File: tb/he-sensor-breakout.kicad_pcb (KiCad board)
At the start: 2 copper layers, 19.1 x 17.8 mm, 28 parts, among them J1 Conn_01x01_Pin, J10 Conn_01x01_Pin, J11 Conn_01x01_Pin, J12 Conn_01x01_Pin, J13 Conn_01x01_Pin, J14 Conn_01x01_Pin, J2 Conn_01x01_Pin, J3 Conn_01x01_Pin, J4 Conn_01x01_Pin, J5 Conn_01x01_Pin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

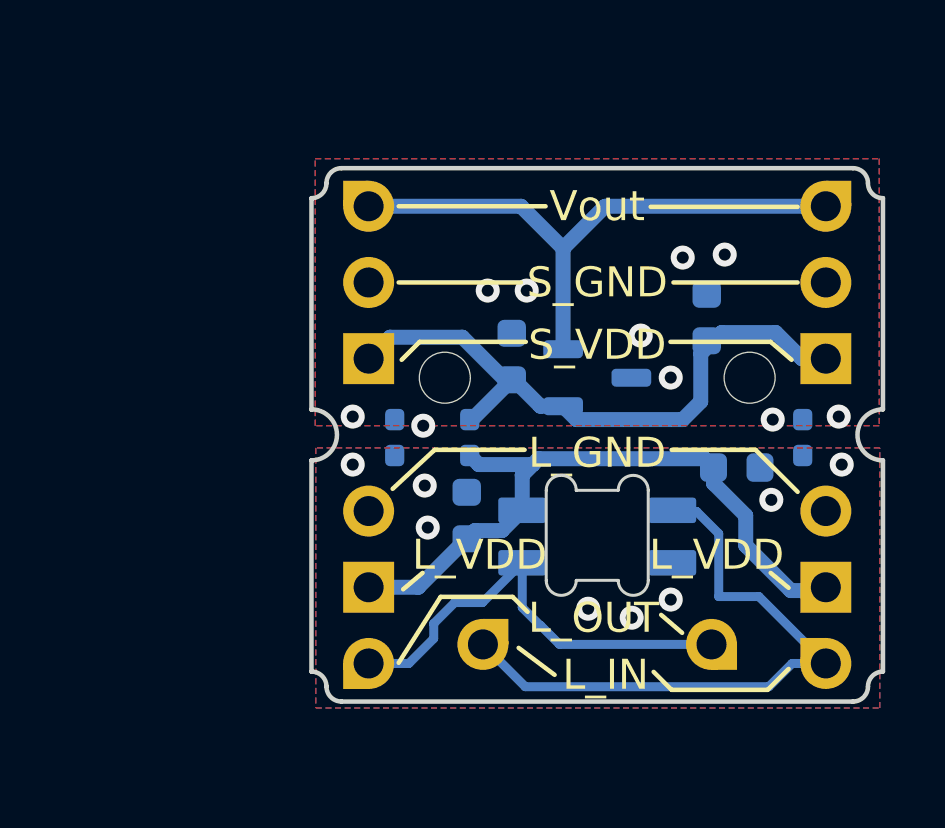
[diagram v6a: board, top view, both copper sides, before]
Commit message: fix edge cuts
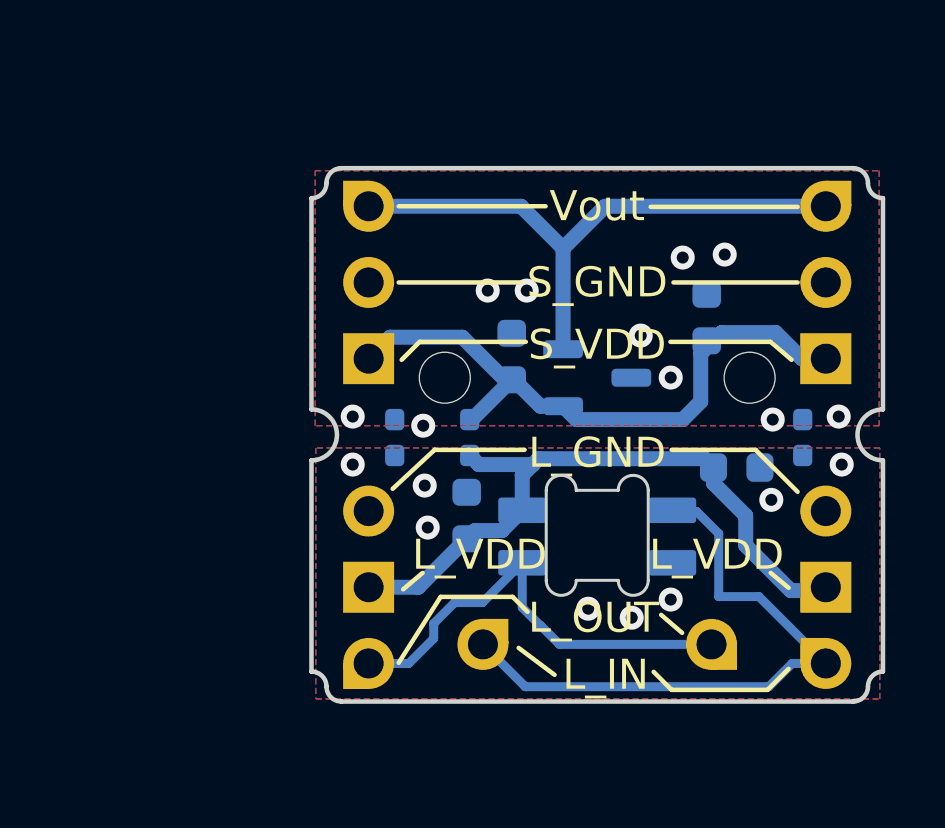
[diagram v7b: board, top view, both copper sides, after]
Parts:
- added REF**: Tab, kikit:Tab, F.Cu at (99.1, 97.2)
- added REF**: Tab, kikit:Tab, F.Cu at (99.1, 106.0)
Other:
- outline, holes or cut-outs redrawn
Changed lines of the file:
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@@
         (effects (font (size 1.2 1.2) (thickness 0.2)))
     )
-    (fp_text user "KIKIT: width: 6.5mm" (at -6.7 2.0275 180) (layer "Dwgs.User")
+    (fp_text user "KIKIT: width: 6mm" (at -6.7 2.0275 180) (layer "Dwgs.User")
         (effects (font (size 1 1) (thickness 0.15)))
     )
@@
   )
   (footprint "kikit:Tab" (layer "F.Cu")
-    (at 120.22 97.2225 180)
+    (at 99.06 97.23)
     (descr "A symbol representing annotation for tab placement")
     (attr exclude_from_pos_files exclude_from_bom)
@@
         (effects (font (size 1.2 1.2) (thickness 0.2)))
     )
-    (fp_text user "KIKIT: width: 6.5mm" (at -6.7 2.0275 180) (layer "Dwgs.User")
+    (fp_text user "KIKIT: width: 6mm" (at -6.7 2.0275) (layer "Dwgs.User")
+        (effects (font (size 1 1) (thickness 0.15)))
+    )
+    (fp_line (start 0.25 0) (end -2.75 0)
+      (stroke (width 0.3) (type solid)) (layer "Dwgs.User"))
+    (fp_line (start 0.25 0) (end -0.75 -1)
+      (stroke (width 0.3) (type solid)) (layer "Dwgs.User"))
+    (fp_line (start 0.25 0) (end -0.75 1)
+      (stroke (width 0.3) (type solid)) (layer "Dwgs.User"))
+    (fp_line (start 0.25 1) (end 0.25 -1)
+      (stroke (width 0.3) (type solid)) (layer "Dwgs.User"))
+  )
+  (footprint "kikit:Tab" (layer "F.Cu")
+    (at 99.06 105.97)
+    (descr "A symbol representing annotation for tab placement")
+    (attr exclude_from_pos_files exclude_from_bom)
+    (fp_text reference "REF**" (at 0 -2) (layer "F.SilkS") hide
+        (effects (font (size 1 1) (thickness 0.15)))
+    )
+    (fp_text value "Tab" (at -3 -1.0725) (layer "Dwgs.User")
+        (effects (font (size 1.2 1.2) (thickness 0.2)))
+    )
+    (fp_text user "KIKIT: width: 6mm" (at -6.7 2.0275) (layer "Dwgs.User")
+        (effects (font (size 1 1) (thickness 0.15)))
+    )
+    (fp_line (start 0.25 0) (end -2.75 0)
+      (stroke (width 0.3) (type solid)) (layer "Dwgs.User"))
+    (fp_line (start 0.25 0) (end -0.75 -1)
+      (stroke (width 0.3) (type solid)) (layer "Dwgs.User"))
+    (fp_line (start 0.25 0) (end -0.75 1)
+      (stroke (width 0.3) (type solid)) (layer "Dwgs.User"))
+    (fp_line (start 0.25 1) (end 0.25 -1)
+      (stroke (width 0.3) (type solid)) (layer "Dwgs.User"))
+  )
+  (footprint "kikit:Tab" (layer "F.Cu")
+    (at 120.22 97.23 180)
+    (descr "A symbol representing annotation for tab placement")
+    (attr exclude_from_pos_files exclude_from_bom)
+    (fp_text reference "REF**" (at 0 -2) (layer "F.SilkS") hide
+        (effects (font (size 1 1) (thickness 0.15)))
+    )
+    (fp_text value "Tab" (at -3 -1.0725) (layer "Dwgs.User")
+        (effects (font (size 1.2 1.2) (thickness 0.2)))
+    )
+    (fp_text user "KIKIT: width: 6mm" (at -6.7 2.0275 180) (layer "Dwgs.User")
         (effects (font (size 1 1) (thickness 0.15)))
     )
@@
   (gr_arc (start 118.745 102.45) (mid 117.895 101.6) (end 118.745 100.75)
     (stroke (width 0.15) (type default)) (layer "Edge.Cuts"))
-  (gr_line (start 99.695 93.71) (end 99.695 100.765)
+  (gr_line (start 99.695 93.71) (end 99.695 100.75)
     (stroke (width 0.15) (type default)) (layer "Edge.Cuts"))
   (gr_line (start 117.745 110.49) (end 100.695 110.49)
@@
       (pts
         (xy 99.84 102.034567)
-        (xy 99.84 110.704567)
-        (xy 118.64 110.704567)
+        (xy 99.84 110.404567)
+        (xy 118.64 110.404567)
         (xy 118.64 102.034567)
       )
@@
     (polygon
       (pts
-        (xy 99.82 92.394567)
-        (xy 118.62 92.394567)
+        (xy 99.82 92.794567)
+        (xy 118.62 92.794567)
         (xy 118.62 101.294567)
         (xy 99.82 101.294567)

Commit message: remove duplicate tabs
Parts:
- removed the REF** at (99.1, 97.2)
- removed the REF** at (99.1, 106.0)
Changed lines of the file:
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@@
-  )
-  (footprint "kikit:Tab" (layer "F.Cu")
-    (at 99.06 97.23)
-    (descr "A symbol representing annotation for tab placement")
-    (attr exclude_from_pos_files exclude_from_bom)
-    (fp_text reference "REF**" (at 0 -2) (layer "F.SilkS") hide
-        (effects (font (size 1 1) (thickness 0.15)))
-    )
-    (fp_text value "Tab" (at -3 -1.0725) (layer "Dwgs.User")
-        (effects (font (size 1.2 1.2) (thickness 0.2)))
-    )
-    (fp_text user "KIKIT: width: 6mm" (at -6.7 2.0275) (layer "Dwgs.User")
-        (effects (font (size 1 1) (thickness 0.15)))
-    )
-    (fp_line (start 0.25 0) (end -2.75 0)
-      (stroke (width 0.3) (type solid)) (layer "Dwgs.User"))
-    (fp_line (start 0.25 0) (end -0.75 -1)
-      (stroke (width 0.3) (type solid)) (layer "Dwgs.User"))
-    (fp_line (start 0.25 0) (end -0.75 1)
-      (stroke (width 0.3) (type solid)) (layer "Dwgs.User"))
-    (fp_line (start 0.25 1) (end 0.25 -1)
-      (stroke (width 0.3) (type solid)) (layer "Dwgs.User"))
-  )
-  (footprint "kikit:Tab" (layer "F.Cu")
-    (at 99.06 105.97)
-    (descr "A symbol representing annotation for tab placement")
-    (attr exclude_from_pos_files exclude_from_bom)
-    (fp_text reference "REF**" (at 0 -2) (layer "F.SilkS") hide
-        (effects (font (size 1 1) (thickness 0.15)))
-    )
-    (fp_text value "Tab" (at -3 -1.0725) (layer "Dwgs.User")
-        (effects (font (size 1.2 1.2) (thickness 0.2)))
-    )
-    (fp_text user "KIKIT: width: 6mm" (at -6.7 2.0275) (layer "Dwgs.User")
-        (effects (font (size 1 1) (thickness 0.15)))
-    )
-    (fp_line (start 0.25 0) (end -2.75 0)
-      (stroke (width 0.3) (type solid)) (layer "Dwgs.User"))
-    (fp_line (start 0.25 0) (end -0.75 -1)
-      (stroke (width 0.3) (type solid)) (layer "Dwgs.User"))
-    (fp_line (start 0.25 0) (end -0.75 1)
-      (stroke (width 0.3) (type solid)) (layer "Dwgs.User"))
-    (fp_line (start 0.25 1) (end 0.25 -1)
-      (stroke (width 0.3) (type solid)) (layer "Dwgs.User"))
   )
   (footprint "kikit:Tab" (layer "F.Cu")
